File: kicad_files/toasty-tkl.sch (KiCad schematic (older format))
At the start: 204 parts, among them CON1 USB-MINI-B, Q1 FET_N, SW0:0 ESC, SW0:10 F9, SW0:11 F10, SW0:12 F11, SW0:13 F12, SW0:14 PRINT, SW0:15 SCROLL LOCK, SW0:2 F1, SW0:3 F2, SW0:4 F3, SW0:5 F4, SW0:6 F5, SW0:7 F6, SW0:8 F7, SW0:9 F8, SW1:0 `, SW1:1 1, SW1:10 0, SW1:11 -, SW1:12 =, SW1:13 BACK SPACE, SW1:14 INSERT, SW1:15 HOME, SW1:2 2, SW1:3 3, SW1:4 4, SW1:5 5, SW1:6 6, SW1:7 7, SW1:8 8, SW1:9 9, SW2:0 TAB, SW2:1 Q, SW2:10 P, SW2:11 [, SW2:12 ], SW2:13 \\, SW2:14 DELETE, SW2:15 END, SW2:2 W, SW2:3 E, SW2:4 R, SW2:5 T, SW2:6 Y, SW2:7 U, SW2:8 I, SW2:9 O, SW3:0 CAPS LOCK, SW3:1 A, SW3:10 ;, SW3:11 ', SW3:13 ENTER, SW3:14 PAGE UP, SW3:15 PAUSE, SW3:2 S, SW3:3 D, SW3:4 F, SW3:5 G, SW3:6 H, SW3:7 J, SW3:8 K, SW3:9 L, SW4:0 LEFT SHIFT, SW4:1 Z, SW4:10 /, SW4:13 RIGHT SHIFT, SW4:14 PAGE DOWN, SW4:15 UP, SW4:2 X, SW4:3 C, SW4:4 V, SW4:5 B, SW4:6 N, SW4:7 M, SW4:8 ,, SW4:9 ., SW5:0 LEFT CTRL, SW5:1 LEFT WINDOWS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

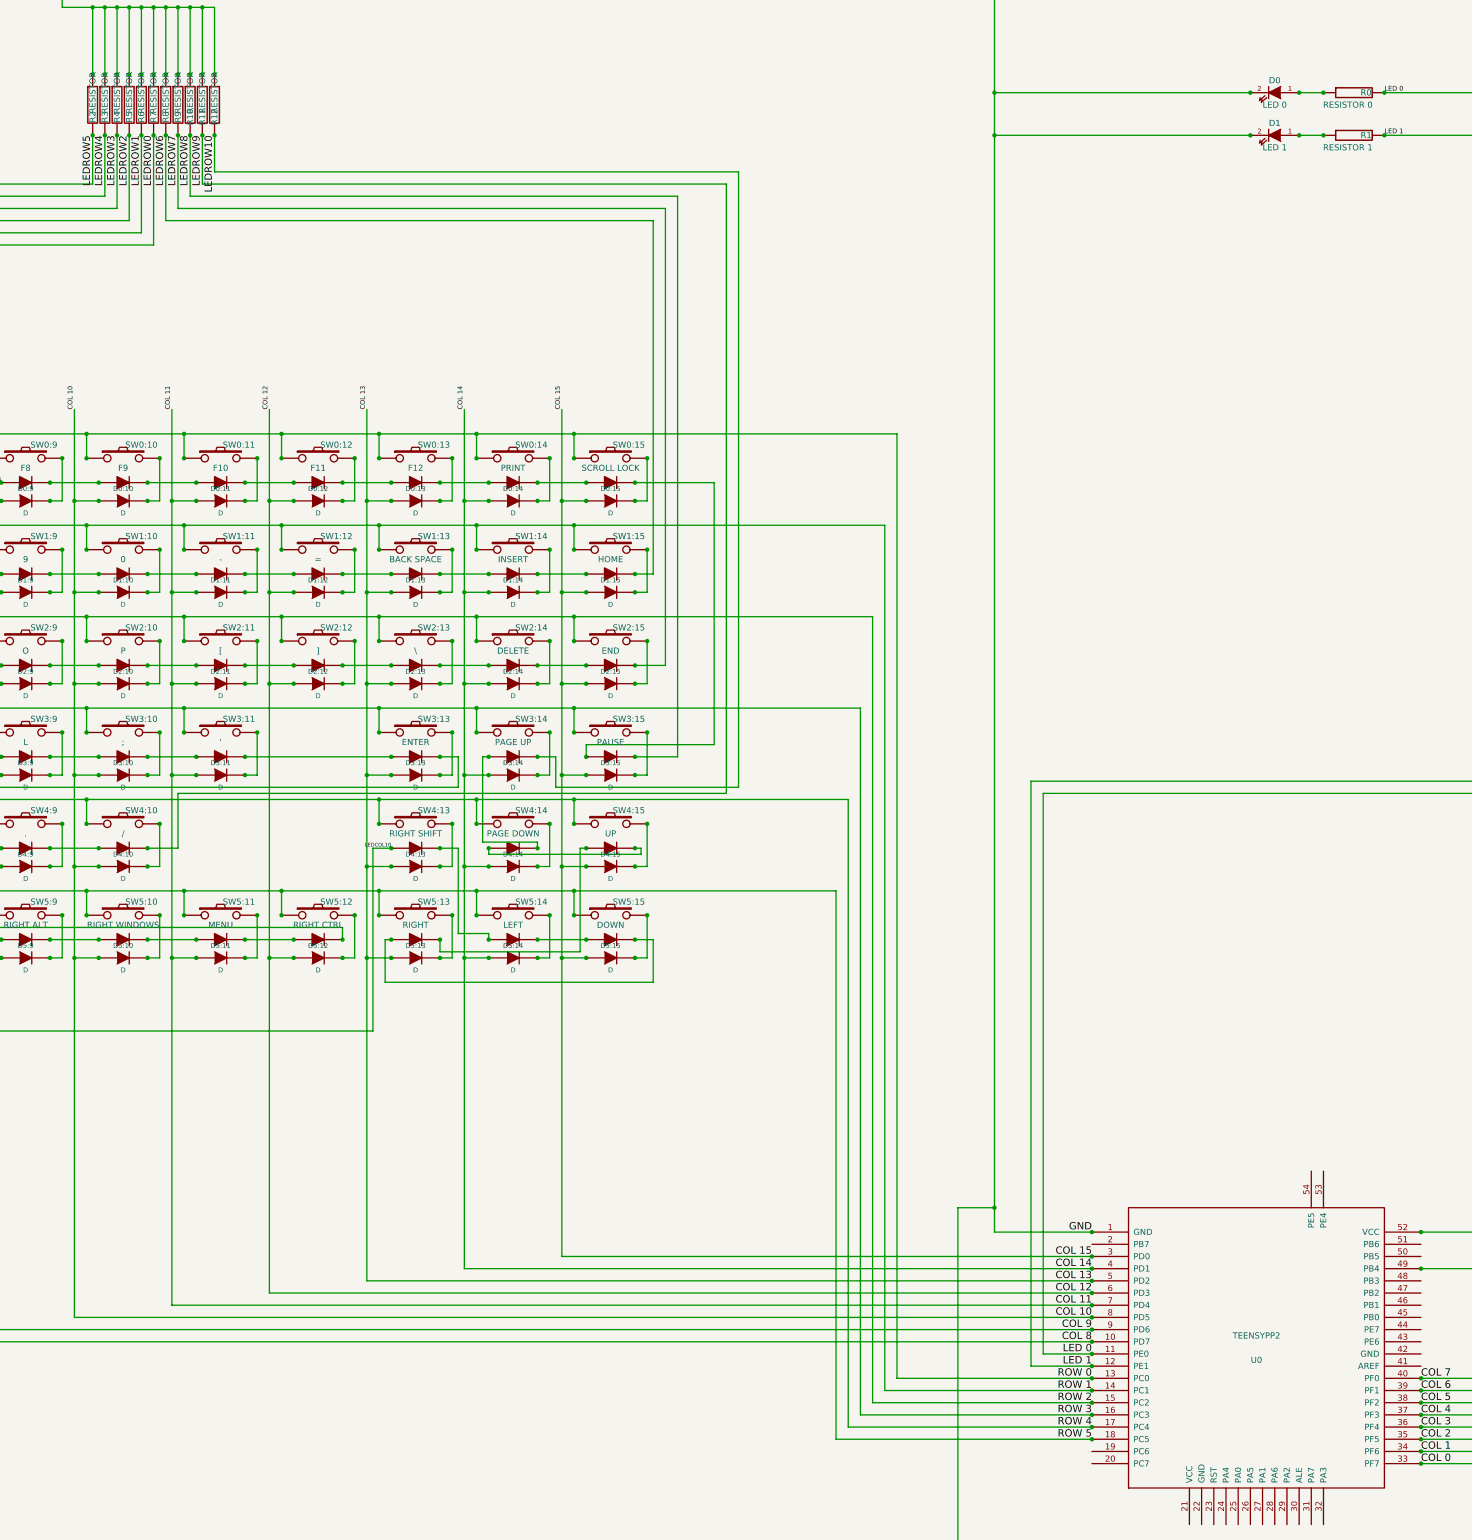
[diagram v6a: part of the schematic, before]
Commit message: Finished parts list, fixed LED notes. double checked all parts, flipped boost converter parts all to rear of PCB.
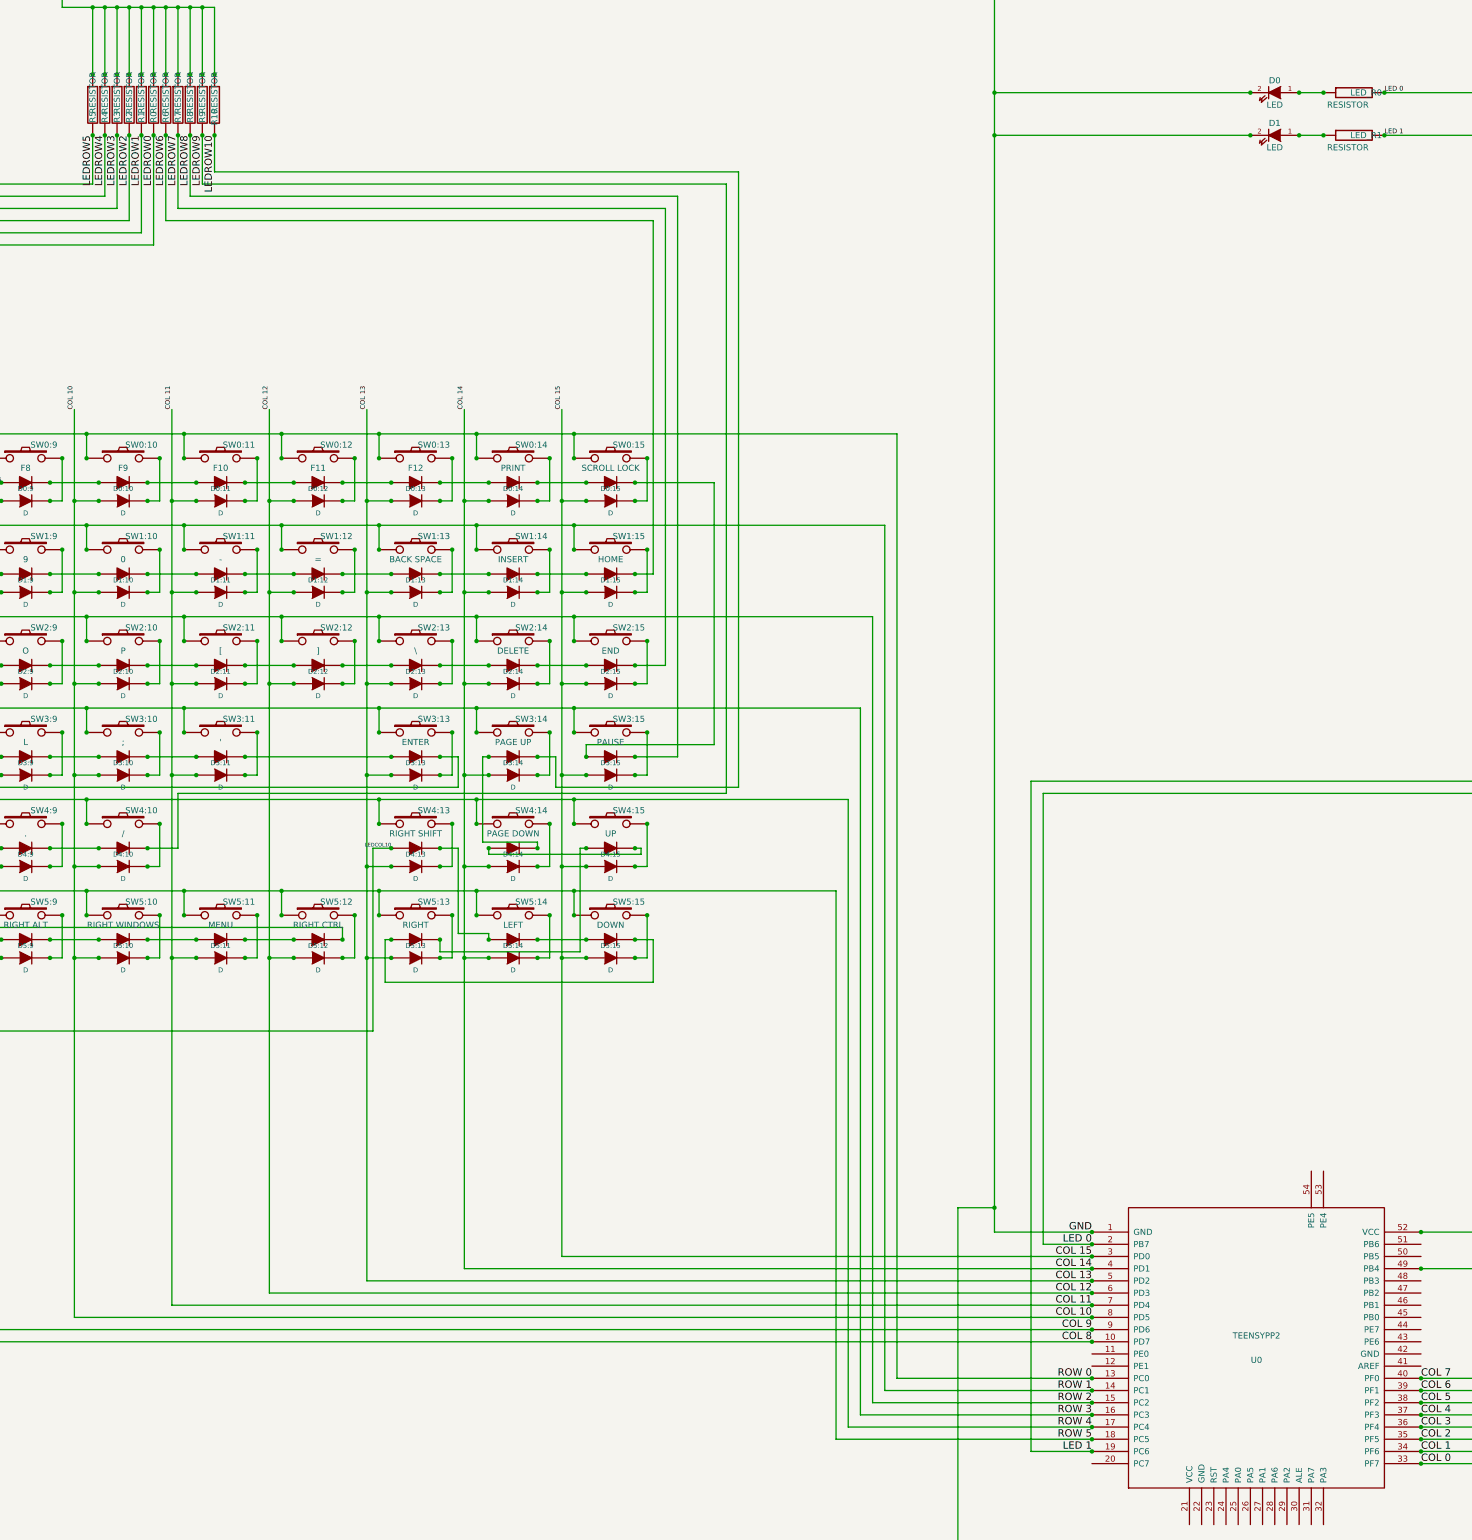
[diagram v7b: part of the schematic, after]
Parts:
- D0: value LED 0 -> LED
- D1: value LED 1 -> LED
- LED_R0: renamed from R0; value RESISTOR 0 -> RESISTOR
- LED_R1: renamed from R1; value RESISTOR 1 -> RESISTOR
- renumbered R7 to R0, R6 to R1, R12 to R10, R5 to R2, R4 to R3, R3 to R4, R2 to R5, R8 to R6, R9 to R7, R10 to R8, R11 to R9
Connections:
- net LED 0: now also U0.2 (PB7); no longer U0.11 (PE0)
- net LED 1: now also U0.19 (PC6); no longer U0.12 (PE1)
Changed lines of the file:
@@
-EESchema Schematic File Version 2
+EESchema Schematic File Version 2  date 01/07/2013 3:49:02 PM
 LIBS:components
 LIBS:toasty-tkl-cache
@@
 Sheet 1 1
 Title "Toasty TKL"
-Date "27 jun 2013"
+Date "1 jul 2013"
 Rev "REV 1A"
 Comp ""
@@
 Text Label 17600 9400 2    60   ~ 0
 ROW 5
-Text Label 17600 8700 2    60   ~ 0
+Text Label 17600 7800 2    60   ~ 0
 LED 0
-Text Label 17600 8800 2    60   ~ 0
+Text Label 17600 9500 2    60   ~ 0
 LED 1
 Text Label 20300 9600 0    60   ~ 0
@@
 COL 15
 $Comp
-L RESISTOR R0
+L RESISTOR LED_R0
 U 1 1 518D7F68
 P 19750 -1650
-F 0 "R0" V 19750 -1750 50  0000 C CNN
-F 1 "RESISTOR 0" V 19850 -1600 50  0000 C CNN
+F 0 "LED_R0" V 19750 -1750 50  0000 C CNN
+F 1 "RESISTOR" V 19850 -1600 50  0000 C CNN
 F 2 "" H 19750 -1650 60  0000 C CNN
 F 3 "" H 19750 -1650 60  0000 C CNN
@@
 P 19100 -1650
 F 0 "D0" H 19100 -1550 50  0000 C CNN
-F 1 "LED 0" H 19100 -1750 50  0000 C CNN
+F 1 "LED" H 19100 -1750 50  0000 C CNN
 F 2 "" H 19100 -1650 60  0000 C CNN
 F 3 "" H 19100 -1650 60  0000 C CNN
@@
 LED 1
 $Comp
-L RESISTOR R1
+L RESISTOR LED_R1
 U 1 1 518D7FD5
 P 19750 -1300
-F 0 "R1" V 19750 -1400 50  0000 C CNN
-F 1 "RESISTOR 1" V 19850 -1250 50  0000 C CNN
+F 0 "LED_R1" V 19750 -1400 50  0000 C CNN
+F 1 "RESISTOR" V 19850 -1250 50  0000 C CNN
 F 2 "" H 19750 -1300 60  0000 C CNN
 F 3 "" H 19750 -1300 60  0000 C CNN
@@
 P 19100 -1300
 F 0 "D1" H 19100 -1200 50  0000 C CNN
-F 1 "LED 1" H 19100 -1400 50  0000 C CNN
+F 1 "LED" H 19100 -1400 50  0000 C CNN
 F 2 "" H 19100 -1300 60  0000 C CNN
 F 3 "" H 19100 -1300 60  0000 C CNN
@@
 $EndComp
 $Comp
-L RESISTOR R2
+L RESISTOR R5
 U 1 1 519C4382
 P 9400 -1550
-F 0 "R2" V 9400 -1650 50  0000 C CNN
+F 0 "R5" V 9400 -1650 50  0000 C CNN
 F 1 "RESISTOR" V 9400 -1450 50  0000 C CNN
 F 2 "" H 9400 -1550 60  0000 C CNN
@@
 $EndComp
 $Comp
-L RESISTOR R3
+L RESISTOR R4
 U 1 1 519C4391
 P 9500 -1550
-F 0 "R3" V 9500 -1650 50  0000 C CNN
+F 0 "R4" V 9500 -1650 50  0000 C CNN
 F 1 "RESISTOR" V 9500 -1450 50  0000 C CNN
 F 2 "" H 9500 -1550 60  0000 C CNN
@@
 $EndComp
 $Comp
-L RESISTOR R4
+L RESISTOR R3
 U 1 1 519C43B9
 P 9600 -1550
-F 0 "R4" V 9600 -1650 50  0000 C CNN
+F 0 "R3" V 9600 -1650 50  0000 C CNN
 F 1 "RESISTOR" V 9600 -1450 50  0000 C CNN
 F 2 "" H 9600 -1550 60  0000 C CNN
@@
 $EndComp
 $Comp
-L RESISTOR R5
+L RESISTOR R2
 U 1 1 519C43D2
 P 9700 -1550
-F 0 "R5" V 9700 -1650 50  0000 C CNN
+F 0 "R2" V 9700 -1650 50  0000 C CNN
 F 1 "RESISTOR" V 9700 -1450 50  0000 C CNN
 F 2 "" H 9700 -1550 60  0000 C CNN
@@
 $EndComp
 $Comp
-L RESISTOR R6
+L RESISTOR R1
 U 1 1 519C43EB
 P 9800 -1550
-F 0 "R6" V 9800 -1650 50  0000 C CNN
+F 0 "R1" V 9800 -1650 50  0000 C CNN
 F 1 "RESISTOR" V 9800 -1450 50  0000 C CNN
 F 2 "" H 9800 -1550 60  0000 C CNN
@@
 $EndComp
 $Comp
-L RESISTOR R7
+L RESISTOR R0
 U 1 1 519C4404
 P 9900 -1550
-F 0 "R7" V 9900 -1650 50  0000 C CNN
+F 0 "R0" V 9900 -1650 50  0000 C CNN
 F 1 "RESISTOR" V 9900 -1450 50  0000 C CNN
 F 2 "" H 9900 -1550 60  0000 C CNN
@@
 $EndComp
 $Comp
-L RESISTOR R8
+L RESISTOR R6
 U 1 1 519C441D
 P 10000 -1550
-F 0 "R8" V 10000 -1650 50  0000 C CNN
+F 0 "R6" V 10000 -1650 50  0000 C CNN
 F 1 "RESISTOR" V 10000 -1450 50  0000 C CNN
 F 2 "" H 10000 -1550 60  0000 C CNN
@@
 $EndComp
 $Comp
-L RESISTOR R9
+L RESISTOR R7
 U 1 1 519C4436
 P 10100 -1550
-F 0 "R9" V 10100 -1650 50  0000 C CNN
+F 0 "R7" V 10100 -1650 50  0000 C CNN
 F 1 "RESISTOR" V 10100 -1450 50  0000 C CNN
 F 2 "" H 10100 -1550 60  0000 C CNN
@@
 $EndComp
 $Comp
-L RESISTOR R10
+L RESISTOR R8
 U 1 1 519C444F
 P 10200 -1550
-F 0 "R10" V 10200 -1650 50  0000 C CNN
+F 0 "R8" V 10200 -1650 50  0000 C CNN
 F 1 "RESISTOR" V 10200 -1450 50  0000 C CNN
 F 2 "" H 10200 -1550 60  0000 C CNN
@@
 $EndComp
 $Comp
-L RESISTOR R11
+L RESISTOR R9
 U 1 1 519C4468
 P 10300 -1550
-F 0 "R11" V 10300 -1650 50  0000 C CNN
+F 0 "R9" V 10300 -1650 50  0000 C CNN
 F 1 "RESISTOR" V 10300 -1450 50  0000 C CNN
 F 2 "" H 10300 -1550 60  0000 C CNN
@@
 $EndComp
 $Comp
-L RESISTOR R12
+L RESISTOR R10
 U 1 1 519C4481
 P 10400 -1550
-F 0 "R12" V 10400 -1650 50  0000 C CNN
+F 0 "R10" V 10400 -1650 50  0000 C CNN
 F 1 "RESISTOR" V 10400 -1450 50  0000 C CNN
 F 2 "" H 10400 -1550 60  0000 C CNN
@@
 	21150 13300 -2050 13300
 Wire Wire Line
-	17600 8700 17200 8700
-Wire Wire Line
-	17200 8700 17200 4100
-Wire Wire Line
 	17200 4100 21500 4100
 Wire Wire Line
@@
 Wire Wire Line
 	21400 4000 17100 4000
-Wire Wire Line
-	17100 4000 17100 8800
-Wire Wire Line
-	17100 8800 17600 8800
-Connection ~ 17600 8700
-Connection ~ 17600 8800
 Connection ~ 20300 7700
 Wire Wire Line
@@
 Wire Wire Line
 	10400 -2350 10400 -1800
+Wire Wire Line
+	17600 7800 17200 7800
+Wire Wire Line
+	17200 7800 17200 4100
+Connection ~ 17600 7800
+Connection ~ 17600 9500
+Wire Wire Line
+	17100 4000 17100 9500
+Wire Wire Line
+	17100 9500 17600 9500
 $EndSCHEMATC

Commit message: Cleaned up schematic around boost converter
Edited for clarity and corrected one layout error (inductor/schottky
connection)
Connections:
- net LEDCOL0: now also BC_R1.1, BC_R2.2; no longer BC_R2.1
- net at BC_L1.2, VREG1.1 (Sw_Coll): now also BC_D1.1 (A)
- net at BC_L1.1, BC_R0.1, BC_Rsc1.2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: no longer BC_D1.1 (A)
- new net: BC_R2.1, VREG1.5 (V_Sense)
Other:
- moved on the sheet: BC_Co1, BC_D1, BC_F1, BC_L1, BC_R0, BC_R1, BC_R2
